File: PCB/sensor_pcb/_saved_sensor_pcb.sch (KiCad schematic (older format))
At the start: 3 parts, among them P1 CONN_01X03, Q1 BUT11A

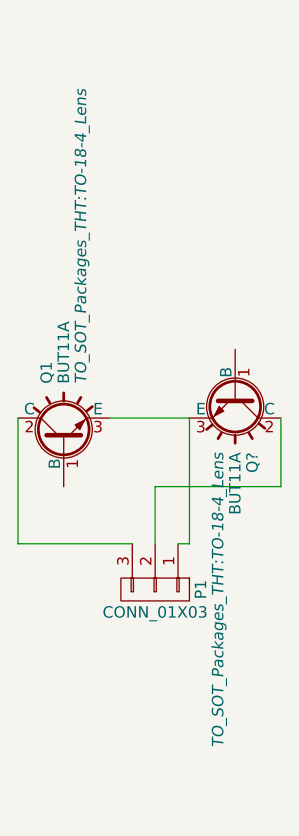
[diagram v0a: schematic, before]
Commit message: Updated sensor pcb to use nte3037 part
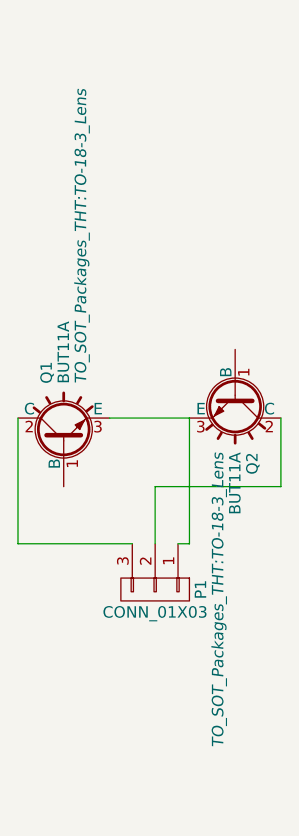
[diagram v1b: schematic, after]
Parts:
- Q1: footprint TO_SOT_Packages_THT:TO-18-4_Lens -> TO_SOT_Packages_THT:TO-18-3_Lens
- Q2: renamed from Q?; footprint TO_SOT_Packages_THT:TO-18-4_Lens -> TO_SOT_Packages_THT:TO-18-3_Lens
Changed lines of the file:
@@
 F 0 "Q1" H 5900 3875 50  0000 L CNN
 F 1 "BUT11A" H 5900 3800 50  0000 L CNN
-F 2 "TO_SOT_Packages_THT:TO-18-4_Lens" H 5900 3725 50  0000 L CIN
+F 2 "TO_SOT_Packages_THT:TO-18-3_Lens" H 5900 3725 50  0000 L CIN
 F 3 "" H 5650 3800 50  0000 L CNN
 	1    5650 3800
@@
 $EndComp
 $Comp
-L BUT11A Q?
+L BUT11A Q2
 U 1 1 596CC336
 P 6400 3600
-F 0 "Q?" H 6650 3675 50  0000 L CNN
+F 0 "Q2" H 6650 3675 50  0000 L CNN
 F 1 "BUT11A" H 6650 3600 50  0000 L CNN
-F 2 "TO_SOT_Packages_THT:TO-18-4_Lens" H 6650 3525 50  0000 L CIN
+F 2 "TO_SOT_Packages_THT:TO-18-3_Lens" H 6650 3525 50  0000 L CIN
 F 3 "" H 6400 3600 50  0000 L CNN
 	1    6400 3600
